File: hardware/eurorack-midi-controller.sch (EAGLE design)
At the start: 7 parts, among them Q1 2N3904, U1 THONKICONNNEW, U2 328P

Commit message: started building schematic.
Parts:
- added R4, R5: 10K, ESSY:RESISTOR_HORZ
- added S1: ENCODER-SWITCH, SparkFun-Switches:ENCODER-SWITCH
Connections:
- new net ENCODER_SWITCH: R5.2, S1.SW-
- new net N$6: MCP1.RESET, R4.1
- net 3.3V: now also MCP1.A0, MCP1.A1, MCP1.A2, MCP1.GND, R5.1
- net 5V: now also MCP1.POWER, R4.2, S1.SW+
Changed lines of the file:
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@@
 <part name="U2" library="SparkFun-IC-Microcontroller" deviceset="ATMEGA328P_PDIP" device="" value="328P"/>
 <part name="MCP1" library="ESSY" deviceset="MCP23017_DIP" device=""/>
+<part name="U$4" library="ESSY" deviceset="PWR" device="" value="+5V"/>
+<part name="U$5" library="ESSY" deviceset="GND" device=""/>
+<part name="U$6" library="ESSY" deviceset="GND" device=""/>
+<part name="R4" library="ESSY" deviceset="RESISTOR_HORZ" device="" value="10K"/>
+<part name="U$7" library="ESSY" deviceset="PWR" device="" value="+5V"/>
+<part name="S1" library="SparkFun-Switches" deviceset="ENCODER-SWITCH" device=""/>
+<part name="U$8" library="ESSY" deviceset="PWR" device="" value="+5V"/>
+<part name="U$9" library="ESSY" deviceset="GND" device=""/>
+<part name="R5" library="ESSY" deviceset="RESISTOR_HORZ" device="" value="10K"/>
 </parts>
 <sheets>
@@
 <instance part="U2" gate="U1" x="93.98" y="58.42"/>
 <instance part="MCP1" gate="G$1" x="116.84" y="-35.56"/>
+<instance part="U$4" gate="G$1" x="60.96" y="-35.56" rot="R90"/>
+<instance part="U$5" gate="G$1" x="48.26" y="-38.1" rot="R270"/>
+<instance part="U$6" gate="G$1" x="129.54" y="-48.26" rot="R90"/>
+<instance part="R4" gate="G$1" x="132.08" y="-40.64"/>
+<instance part="U$7" gate="G$1" x="142.24" y="-40.64" rot="R270"/>
+<instance part="S1" gate="G$1" x="190.5" y="50.8"/>
+<instance part="U$8" gate="G$1" x="172.72" y="55.88" rot="R90"/>
+<instance part="U$9" gate="G$1" x="170.18" y="25.4"/>
+<instance part="R5" gate="G$1" x="170.18" y="35.56" rot="R90"/>
 </instances>
 <busses>
@@
 <pinref part="U$1" gate="G$1" pin="3.3V"/>
 <wire x1="-15.24" y1="53.34" x2="-15.24" y2="45.72" width="0.1524" layer="91"/>
+</segment>
+<segment>
+<pinref part="MCP1" gate="G$1" pin="GND"/>
+<pinref part="U$5" gate="G$1" pin="3.3V"/>
+<wire x1="76.2" y1="-38.1" x2="50.8" y2="-38.1" width="0.1524" layer="91"/>
+</segment>
+<segment>
+<pinref part="MCP1" gate="G$1" pin="A0"/>
+<pinref part="U$6" gate="G$1" pin="3.3V"/>
+<wire x1="109.22" y1="-48.26" x2="116.84" y2="-48.26" width="0.1524" layer="91"/>
+<pinref part="MCP1" gate="G$1" pin="A1"/>
+<wire x1="116.84" y1="-48.26" x2="119.38" y2="-48.26" width="0.1524" layer="91"/>
+<wire x1="119.38" y1="-48.26" x2="127" y2="-48.26" width="0.1524" layer="91"/>
+<wire x1="109.22" y1="-45.72" x2="116.84" y2="-45.72" width="0.1524" layer="91"/>
+<wire x1="116.84" y1="-45.72" x2="116.84" y2="-48.26" width="0.1524" layer="91"/>
+<junction x="116.84" y="-48.26"/>
+<pinref part="MCP1" gate="G$1" pin="A2"/>
+<wire x1="109.22" y1="-43.18" x2="119.38" y2="-43.18" width="0.1524" layer="91"/>
+<wire x1="119.38" y1="-43.18" x2="119.38" y2="-48.26" width="0.1524" layer="91"/>
+<junction x="119.38" y="-48.26"/>
+</segment>
+<segment>
+<pinref part="R5" gate="G$1" pin="1"/>
+<pinref part="U$9" gate="G$1" pin="3.3V"/>
+<wire x1="170.18" y1="30.48" x2="170.18" y2="27.94" width="0.1524" layer="91"/>
 </segment>
 </net>
@@
 <wire x1="-15.24" y1="83.82" x2="-15.24" y2="91.44" width="0.1524" layer="91"/>
 </segment>
+<segment>
+<pinref part="MCP1" gate="G$1" pin="POWER"/>
+<pinref part="U$4" gate="G$1" pin="5V"/>
+<wire x1="76.2" y1="-35.56" x2="60.96" y2="-35.56" width="0.1524" layer="91"/>
+</segment>
+<segment>
+<pinref part="U$7" gate="G$1" pin="5V"/>
+<pinref part="R4" gate="G$1" pin="2"/>
+<wire x1="142.24" y1="-40.64" x2="137.16" y2="-40.64" width="0.1524" layer="91"/>
+</segment>
+<segment>
+<pinref part="S1" gate="G$1" pin="SW+"/>
+<pinref part="U$8" gate="G$1" pin="5V"/>
+<wire x1="180.34" y1="55.88" x2="172.72" y2="55.88" width="0.1524" layer="91"/>
+</segment>
 </net>
 <net name="TRIG_IN_A" class="0">
@@
 </segment>
 </net>
+<net name="N$6" class="0">
+<segment>
+<pinref part="R4" gate="G$1" pin="1"/>
+<pinref part="MCP1" gate="G$1" pin="RESET"/>
+<wire x1="127" y1="-40.64" x2="109.22" y2="-40.64" width="0.1524" layer="91"/>
+</segment>
+</net>
+<net name="ENCODER_SWITCH" class="0">
+<segment>
+<pinref part="S1" gate="G$1" pin="SW-"/>
+<wire x1="180.34" y1="45.72" x2="170.18" y2="45.72" width="0.1524" layer="91"/>
+<pinref part="R5" gate="G$1" pin="2"/>
+<wire x1="170.18" y1="45.72" x2="170.18" y2="40.64" width="0.1524" layer="91"/>
+<wire x1="170.18" y1="45.72" x2="160.02" y2="45.72" width="0.1524" layer="91"/>
+<junction x="170.18" y="45.72"/>
+<label x="160.02" y="45.72" size="1.016" layer="95" rot="R180" xref="yes"/>
+</segment>
+</net>

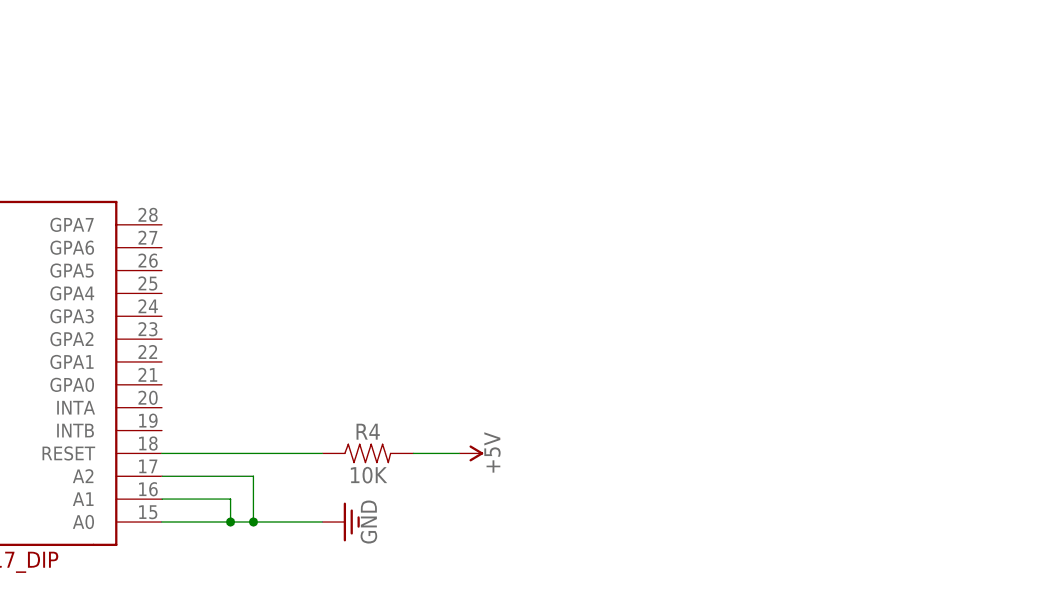
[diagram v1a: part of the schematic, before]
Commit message: completed the MIDI clock implementation for syncing live.
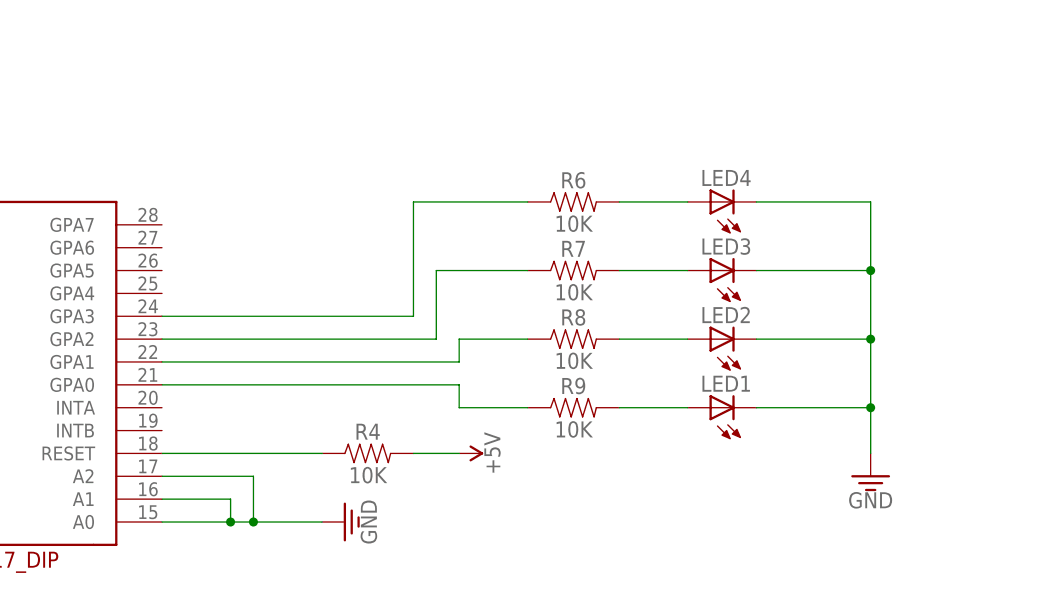
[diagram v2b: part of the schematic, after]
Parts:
- added LED1, LED2, LED3, LED4: (no value), led:LED3MM
- added R6, R7, R8, R9: 10K, ESSY:RESISTOR_HORZ
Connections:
- new net N$10: LED4.A, R6.2
- new net N$11: LED3.A, R7.2
- new net N$12: LED2.A, R8.2
- new net N$4: MCP1.GPA0, R9.1
- new net N$5: LED1.A, R9.2
- new net N$7: MCP1.GPA1, R8.1
- new net N$8: MCP1.GPA2, R7.1
- new net N$9: MCP1.GPA3, R6.1
- net 3.3V: now also LED1.C, LED2.C, LED3.C, LED4.C
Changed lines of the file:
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@@
 <part name="U$9" library="ESSY" deviceset="GND" device=""/>
 <part name="R5" library="ESSY" deviceset="RESISTOR_HORZ" device="" value="10K"/>
+<part name="LED1" library="led" library_urn="urn:adsk.eagle:library:259" deviceset="LED" device="3MM" package3d_urn="urn:adsk.eagle:package:15797/1"/>
+<part name="LED2" library="led" library_urn="urn:adsk.eagle:library:259" deviceset="LED" device="3MM" package3d_urn="urn:adsk.eagle:package:15797/1"/>
+<part name="LED3" library="led" library_urn="urn:adsk.eagle:library:259" deviceset="LED" device="3MM" package3d_urn="urn:adsk.eagle:package:15797/1"/>
+<part name="LED4" library="led" library_urn="urn:adsk.eagle:library:259" deviceset="LED" device="3MM" package3d_urn="urn:adsk.eagle:package:15797/1"/>
+<part name="R6" library="ESSY" deviceset="RESISTOR_HORZ" device="" value="10K"/>
+<part name="R7" library="ESSY" deviceset="RESISTOR_HORZ" device="" value="10K"/>
+<part name="R8" library="ESSY" deviceset="RESISTOR_HORZ" device="" value="10K"/>
+<part name="R9" library="ESSY" deviceset="RESISTOR_HORZ" device="" value="10K"/>
+<part name="U$10" library="ESSY" deviceset="GND" device=""/>
 </parts>
 <sheets>
@@
 <instance part="U$9" gate="G$1" x="170.18" y="25.4"/>
 <instance part="R5" gate="G$1" x="170.18" y="35.56" rot="R90"/>
+<instance part="LED1" gate="G$1" x="170.18" y="-35.56" rot="R90"/>
+<instance part="LED2" gate="G$1" x="170.18" y="-27.94" rot="R90"/>
+<instance part="LED3" gate="G$1" x="170.18" y="-20.32" rot="R90"/>
+<instance part="LED4" gate="G$1" x="170.18" y="-12.7" rot="R90"/>
+<instance part="R6" gate="G$1" x="154.94" y="-12.7"/>
+<instance part="R7" gate="G$1" x="154.94" y="-20.32"/>
+<instance part="R8" gate="G$1" x="154.94" y="-27.94"/>
+<instance part="R9" gate="G$1" x="154.94" y="-35.56"/>
+<instance part="U$10" gate="G$1" x="187.96" y="-43.18"/>
 </instances>
 <busses>
@@
 <wire x1="170.18" y1="30.48" x2="170.18" y2="27.94" width="0.1524" layer="91"/>
 </segment>
+<segment>
+<pinref part="LED1" gate="G$1" pin="C"/>
+<wire x1="175.26" y1="-35.56" x2="187.96" y2="-35.56" width="0.1524" layer="91"/>
+<pinref part="U$10" gate="G$1" pin="3.3V"/>
+<wire x1="187.96" y1="-35.56" x2="187.96" y2="-40.64" width="0.1524" layer="91"/>
+<pinref part="LED2" gate="G$1" pin="C"/>
+<wire x1="175.26" y1="-27.94" x2="187.96" y2="-27.94" width="0.1524" layer="91"/>
+<wire x1="187.96" y1="-27.94" x2="187.96" y2="-35.56" width="0.1524" layer="91"/>
+<junction x="187.96" y="-35.56"/>
+<pinref part="LED3" gate="G$1" pin="C"/>
+<wire x1="175.26" y1="-20.32" x2="187.96" y2="-20.32" width="0.1524" layer="91"/>
+<wire x1="187.96" y1="-20.32" x2="187.96" y2="-27.94" width="0.1524" layer="91"/>
+<junction x="187.96" y="-27.94"/>
+<pinref part="LED4" gate="G$1" pin="C"/>
+<wire x1="175.26" y1="-12.7" x2="187.96" y2="-12.7" width="0.1524" layer="91"/>
+<wire x1="187.96" y1="-12.7" x2="187.96" y2="-20.32" width="0.1524" layer="91"/>
+<junction x="187.96" y="-20.32"/>
+</segment>
 </net>
 <net name="N$1" class="0">
@@
 </segment>
 </net>
+<net name="N$4" class="0">
+<segment>
+<pinref part="MCP1" gate="G$1" pin="GPA0"/>
+<wire x1="109.22" y1="-33.02" x2="142.24" y2="-33.02" width="0.1524" layer="91"/>
+<wire x1="142.24" y1="-33.02" x2="142.24" y2="-35.56" width="0.1524" layer="91"/>
+<pinref part="R9" gate="G$1" pin="1"/>
+<wire x1="142.24" y1="-35.56" x2="149.86" y2="-35.56" width="0.1524" layer="91"/>
+</segment>
+</net>
+<net name="N$5" class="0">
+<segment>
+<pinref part="R9" gate="G$1" pin="2"/>
+<pinref part="LED1" gate="G$1" pin="A"/>
+<wire x1="160.02" y1="-35.56" x2="167.64" y2="-35.56" width="0.1524" layer="91"/>
+</segment>
+</net>
+<net name="N$7" class="0">
+<segment>
+<pinref part="MCP1" gate="G$1" pin="GPA1"/>
+<wire x1="109.22" y1="-30.48" x2="142.24" y2="-30.48" width="0.1524" layer="91"/>
+<wire x1="142.24" y1="-30.48" x2="142.24" y2="-27.94" width="0.1524" layer="91"/>
+<pinref part="R8" gate="G$1" pin="1"/>
+<wire x1="142.24" y1="-27.94" x2="149.86" y2="-27.94" width="0.1524" layer="91"/>
+</segment>
+</net>
+<net name="N$8" class="0">
+<segment>
+<pinref part="MCP1" gate="G$1" pin="GPA2"/>
+<wire x1="109.22" y1="-27.94" x2="139.7" y2="-27.94" width="0.1524" layer="91"/>
+<wire x1="139.7" y1="-27.94" x2="139.7" y2="-20.32" width="0.1524" layer="91"/>
+<pinref part="R7" gate="G$1" pin="1"/>
+<wire x1="139.7" y1="-20.32" x2="149.86" y2="-20.32" width="0.1524" layer="91"/>
+</segment>
+</net>
+<net name="N$9" class="0">
+<segment>
+<pinref part="MCP1" gate="G$1" pin="GPA3"/>
+<wire x1="109.22" y1="-25.4" x2="137.16" y2="-25.4" width="0.1524" layer="91"/>
+<wire x1="137.16" y1="-25.4" x2="137.16" y2="-12.7" width="0.1524" layer="91"/>
+<pinref part="R6" gate="G$1" pin="1"/>
+<wire x1="137.16" y1="-12.7" x2="149.86" y2="-12.7" width="0.1524" layer="91"/>
+</segment>
+</net>
+<net name="N$10" class="0">
+<segment>
+<pinref part="R6" gate="G$1" pin="2"/>
+<pinref part="LED4" gate="G$1" pin="A"/>
+<wire x1="160.02" y1="-12.7" x2="167.64" y2="-12.7" width="0.1524" layer="91"/>
+</segment>
+</net>
+<net name="N$11" class="0">
+<segment>
+<pinref part="R7" gate="G$1" pin="2"/>
+<pinref part="LED3" gate="G$1" pin="A"/>
+<wire x1="160.02" y1="-20.32" x2="167.64" y2="-20.32" width="0.1524" layer="91"/>
+</segment>
+</net>
+<net name="N$12" class="0">
+<segment>
+<pinref part="R8" gate="G$1" pin="2"/>
+<pinref part="LED2" gate="G$1" pin="A"/>
+<wire x1="160.02" y1="-27.94" x2="167.64" y2="-27.94" width="0.1524" layer="91"/>
+</segment>
+</net>
 </nets>
 </sheet>
@@
 </drawing>
 <compatibility>
+<note version="8.2" severity="warning">
+Since Version 8.2, EAGLE supports online libraries. The ids
+of those online libraries will not be understood (or retained)
+with this version.
+</note>
 <note version="8.3" severity="warning">
 Since Version 8.3, EAGLE supports URNs for individual library
@@
 will not be understood (or retained) with this version.
 </note>
+<note version="8.3" severity="warning">
+Since Version 8.3, EAGLE supports the association of 3D packages
+with devices in libraries, schematics, and board files. Those 3D
+packages will not be understood (or retained) with this version.
+</note>
 </compatibility>
